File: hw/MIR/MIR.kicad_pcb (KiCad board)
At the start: 2 copper layers, 89.6 x 55 mm, 90 parts, among them J1 CONN_02X08, J10 CONN_01X01, J11 CONN_01X01, J12 CONN_01X01, J13 CONN_01X01, J14 CONN_01X01, J15 CONN_01X01, J16 CONN_01X01, J17 CONN_01X01, J18 CONN_01X01, J19 CONN_01X01, J2 CONN_02X08, J20 CONN_01X01, J21 CONN_01X01, J22 CONN_01X01, J23 CONN_01X01, J24 CONN_01X01, J25 CONN_01X01, J26 CONN_01X01, J27 CONN_01X01, J28 CONN_01X01, J29 CONN_01X01, J3 CONN_01X02, J30 CONN_01X01, J31 CONN_01X01, J32 CONN_01X01, J33 CONN_01X01, J34 CONN_01X01, J35 CONN_01X01, J36 CONN_01X01, J37 CONN_01X01, J38 CONN_01X01, J39 CONN_01X01, J40 CONN_01X01, J41 CONN_02X03, J42 CONN_01X15, J43 CONN_01X15, J44 USB_B_Mini, J9 CONN_01X01, SW1 SwitchPush, U1 ATmega328P-AU, U2 FT230XQ, Y1 16MHz

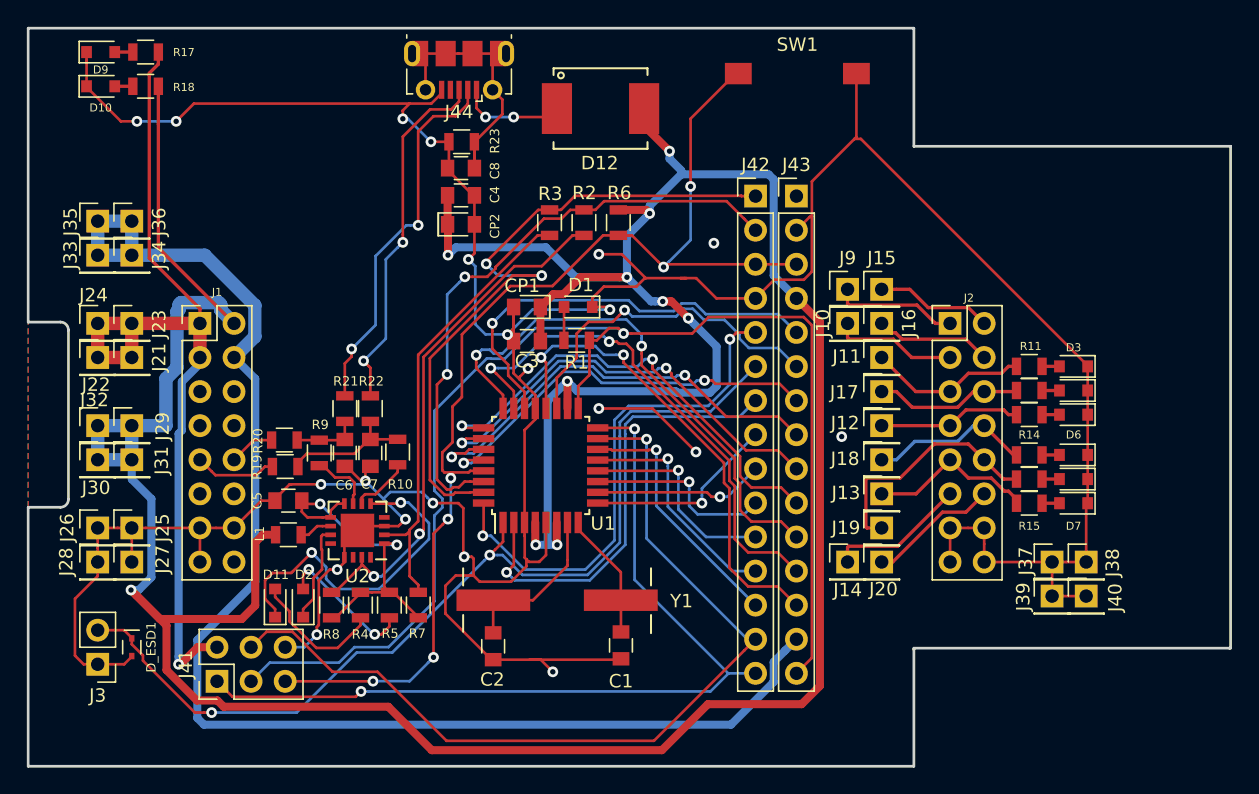
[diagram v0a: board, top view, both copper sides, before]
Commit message: Various fixes in schematics and PCB design
What has been done:

* Change Atmega328p footprint from TQFP to WQFN
* Replace FT230XQ with FT232RQ
* Adapt schematics to new FTDI chip
* Add load resistor for IR LED
* Add missing decoupling capacitors to some VDD pins
* Add cutout for NanoPi microUSB
* Remove unused USB connector
* Remove unused arduino connectors
* Remove not used (for MIR purposees) LEDs indicating state of STM GPIO
* Rename all files to MIR*
* Use only symbols from MIR libraries
* Rearrange texts on F.Mask layer
* Rearrange overlapping texts on F.Silk layer
* Move D_ESD1 further from J3
* Correct SW1 and XTAL footprints

Change-Id: Icd19173fda610c0574442d99b39109bb18bf1090
Signed-off-by: Katarzyna Gorska <k.gorska@samsung.com>
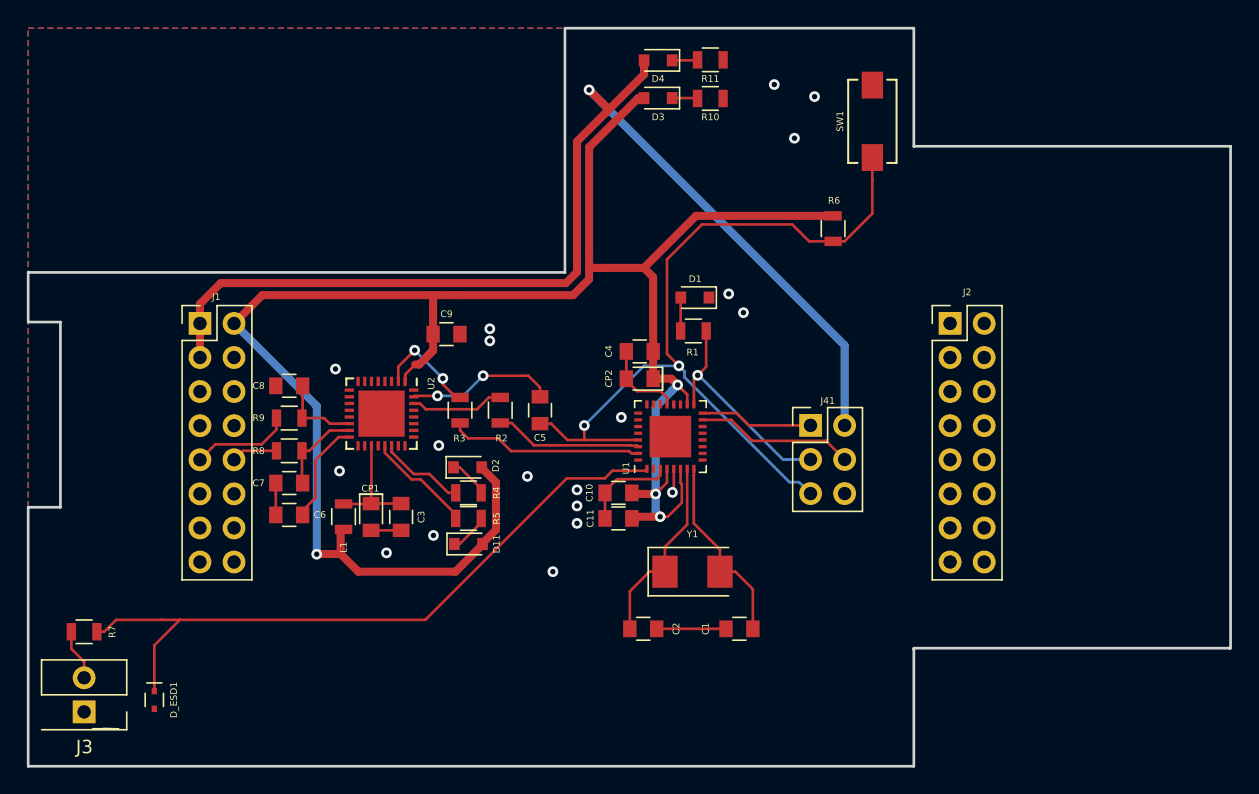
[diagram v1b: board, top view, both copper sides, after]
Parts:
- removed D10, D7: KPT-2012SGC, Diodes_SMD:D_0805
- removed D12: MBRS410L, Muxpi Addon:403AC
- removed D6, D9: KPT-2012EC, Diodes_SMD:D_0805
- removed D8: OSB50805C1E, Diodes_SMD:D_0805
- removed J10, J11, J12, J13, J14, J15, J16, J17, J18, J19, J20, J21, J22, J23, J24, J25, J26, J27, J28, J29, J30, J31, J32, J33, J34, J35, J36, J37, J38, J39, J40, J9: CONN_01X01, Pin_Headers:Pin_Header_Straight_1x01_Pitch2.54mm
- removed J42, J43: CONN_01X15, Muxpi Addon:Pin_Header_Straight_1x15_Pitch2.54mm
- removed J44: USB_B_Mini, Muxpi Addon:USB_Micro-B_Molex-105017-0001
- removed R12, R13, R14, R15, R16, R17, R18: 330R, Resistors_SMD:R_0805
- removed R19, R20, R21, R22: 0, Muxpi Addon:R_0805
- removed R23: 10k, Muxpi Addon:R_0805
- added C10: 0.1uF, MIR:C_0805, F.Cu at (113.3, 169.2)
- added C11: 0.1uF, MIR:C_0805, F.Cu at (113.3, 171.1)
- added C9: 0.1uF, MIR:C_0805, F.Cu at (100.5, 157.4)
- C1, C2, C3, C4, C5: footprint Muxpi Addon:C_0805 -> MIR:C_0805
- C6: value 47pF/50V -> 0.1uF; footprint Muxpi Addon:C_0805 -> MIR:C_0805
- C7: value 47pF/50V -> 47pF; footprint Muxpi Addon:C_0805 -> MIR:C_0805
- C8: value 0.1uF -> 47pF; footprint Muxpi Addon:C_0805 -> MIR:C_0805
- CP1, CP2: footprint Muxpi Addon:C_T_0805 -> MIR:C_T_0805
- D1, D11, D2: footprint Diodes_SMD:D_0805 -> MIR:D_0805
- D3: value KPT-2012EC -> KPT-2012SGC; footprint Diodes_SMD:D_0805 -> MIR:D_0805
- D4: value KPT-2012SGC -> KPT-2012EC; footprint Diodes_SMD:D_0805 -> MIR:D_0805
- D5: value OSB50805C1E -> LED_IR; footprint Diodes_SMD:D_0805 -> MIR:EXTERNAL ELEMENT
- D_ESD1: footprint Muxpi Addon:SOD-523 -> MIR:SOD-523
- J1, J2: footprint Pin_Headers:Pin_Header_Straight_2x08_Pitch2.54mm -> MIR:Pin_Header_Straight_2x08_Pitch2.54mm
- J3: footprint Pin_Headers:Pin_Header_Straight_1x02_Pitch2.54mm -> MIR:Pin_Header_Straight_1x02_Pitch2.54mm_Molex_022232021
- J41: footprint Muxpi Addon:Pin_Header_Straight_2x03_Pitch2.54mm -> MIR:Pin_Header_Straight_2x03_Pitch2.54mm
- L1, R1, R2, R3, R6, R9: footprint Muxpi Addon:R_0805 -> MIR:R_0805
- R10: value 27R -> 330R; footprint Muxpi Addon:R_0805 -> MIR:R_0805
- R11: footprint Resistors_SMD:R_0805 -> MIR:R_0805
- R4, R5: value 560R -> 330R; footprint Muxpi Addon:R_0805 -> MIR:R_0805
- R7: value 10k -> 330R; footprint Muxpi Addon:R_0805 -> MIR:R_0805
- R8: value 10k -> 27R; footprint Muxpi Addon:R_0805 -> MIR:R_0805
- SW1: footprint Muxpi Addon:DTSM-3 -> MIR:DTSM-3
- U1: value ATmega328P-AU -> ATmega328P-MU; footprint Muxpi Addon:TQFP-32_7x7mm_Pitch0.8mm -> MIR:WQFN-32-1EP_5x5mm_Pitch0.5mm
- U2: value FT230XQ -> FT232RQ; footprint Muxpi Addon:QFN-16-1EP_4x4mm_Pitch0.65mm -> MIR:QFN-32-1EP_5x5mm_Pitch0.5mm
- Y1: footprint Muxpi Addon:HC49USM -> MIR:Crystal_SMD_Abracon_ABM3-2pin_5.0x3.2mm_HandSoldering
- moved J41 48.2 mm to (127.6, 164.2), turned to 0 degrees
- moved D4 39.5 mm to (116.2, 137.0)
- moved D5 38.1 mm to (109.5, 157.9), turned to 0 degrees
- moved D3 36.9 mm to (116.2, 139.8)
- moved R10 35.2 mm to (120.1, 139.8), turned to 180 degrees
- moved R11 33.0 mm to (120.1, 137.0), turned to 180 degrees
- moved R7 25.0 mm to (73.5, 179.6), turned to 0 degrees
- moved C8 20.7 mm to (88.8, 161.2), turned to 0 degrees
- moved C5 19.9 mm to (107.4, 163.1), turned to 270 degrees
- moved CP1 19.5 mm to (94.9, 171.0), turned to 270 degrees
- moved C4 17.7 mm to (114.9, 158.7), turned to 180 degrees
- moved CP2 17.6 mm to (114.9, 160.7), turned to 180 degrees
- moved C3 16.1 mm to (97.1, 171.0), turned to 270 degrees
- moved R6 16.0 mm to (129.3, 149.5)
- moved D2 15.9 mm to (102.0, 167.3), turned to 0 degrees
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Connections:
- C3 pad 1: VDD -> /FT_VCC
- C5 pad 2: GND -> /RESET
- C6 pad 1: Net-(C6-Pad1) -> GND
- C6 pad 2: GND -> Net-(C6-Pad2)
- C8 pad 1: Net-(C8-Pad1) -> GND
- C8 pad 2: GND -> Net-(C8-Pad2)
- CP1 pad 1: VDD -> /FT_VCC
- D11 pad 2: Net-(D11-Pad2) -> VDD
- D2 pad 2: Net-(D2-Pad2) -> VDD
- D3 pad 1: GND -> Net-(D3-Pad1)
- D3 pad 2: Net-(D3-Pad2) -> VDD
- D4 pad 1: GND -> Net-(D4-Pad1)
- D4 pad 2: Net-(D4-Pad2) -> +5V
- J1 pad 11: /USB_A+ -> (no net)
- J1 pad 12: /USB_A- -> (no net)
- J1 pad 16: Net-(J1-Pad16) -> (no net)
- J1 pad 4: +3V3 -> (no net)
- J1 pad 5: /SDA -> (no net)
- J1 pad 6: /SCL -> (no net)
- J1 pad 7: /PI_UART_TX -> (no net)
- J1 pad 8: /PI_UART_RX -> (no net)
- J2 pad 1: /SPI_CLK -> (no net)
- J2 pad 10: /ST_GPIO_3 -> (no net)
- J2 pad 11: /ADC1 -> (no net)
- J2 pad 12: /ADC2 -> (no net)
- J2 pad 2: /SPI_MOSI -> (no net)
- J2 pad 3: /SPI_CS -> (no net)
- J2 pad 4: /SPI_MISO -> (no net)
- J2 pad 5: /PI_GPIO_1 -> (no net)
- J2 pad 6: /PI_GPIO_2 -> (no net)
- J2 pad 7: /PI_GPIO_3 -> (no net)
- J2 pad 8: /ST_GPIO_1 -> (no net)
- J2 pad 9: /ST_GPIO_2 -> (no net)
- J3 pad 2: /D3 -> Net-(J3-Pad2)
- L1 pad 1: Net-(L1-Pad1) -> /FT_VCC
- R10 pad 1: Net-(C7-Pad1) -> GND
- R10 pad 2: Net-(R10-Pad2) -> Net-(D3-Pad1)
- R11 pad 1: /PI_GPIO_1 -> GND
- R11 pad 2: Net-(D3-Pad2) -> Net-(D4-Pad1)
- R4 pad 1: Net-(C5-Pad1) -> Net-(R4-Pad1)
- R4 pad 2: Net-(D11-Pad2) -> Net-(D2-Pad1)
- R5 pad 1: Net-(C5-Pad1) -> Net-(R5-Pad1)
- R5 pad 2: Net-(D2-Pad2) -> Net-(D11-Pad1)
- R7 pad 1: /TX -> Net-(J3-Pad2)
- R7 pad 2: Net-(C5-Pad1) -> /D3
- R8 pad 1: /RX -> /USB_B-
- R8 pad 2: Net-(C5-Pad1) -> Net-(C7-Pad1)
- R9 pad 1: Net-(C6-Pad1) -> /USB_B+
- R9 pad 2: Net-(R9-Pad2) -> Net-(C8-Pad2)
- U1 pad 10: /D6 -> (no net)
- U1 pad 11: /D7 -> (no net)
- U1 pad 12: /D8 -> (no net)
- U1 pad 13: /D9 -> (no net)
- U1 pad 14: /D10 -> (no net)
- U1 pad 19: /A6 -> (no net)
- U1 pad 2: /D4 -> (no net)
- U1 pad 20: /AREF -> (no net)
- U1 pad 22: /A7 -> (no net)
- U1 pad 23: /A0 -> (no net)
- U1 pad 24: /A1 -> (no net)
- U1 pad 25: /A2 -> (no net)
- U1 pad 26: /A3 -> (no net)
- U1 pad 27: /A4 -> (no net)
- U1 pad 28: /A5 -> (no net)
- U1 pad 32: /D2 -> (no net)
- U1 pad 9: /D5 -> (no net)
- U2 pad 1: Net-(C5-Pad1) -> VDD
- U2 pad 10: Net-(L1-Pad1) -> (no net)
- U2 pad 11: Net-(D2-Pad1) -> (no net)
- U2 pad 12: Net-(U2-Pad12) -> (no net)
- U2 pad 13: GND -> (no net)
- U2 pad 14: Net-(U2-Pad14) -> Net-(C8-Pad2)
- U2 pad 15: /RX -> Net-(C7-Pad1)
- U2 pad 16: Net-(U2-Pad16) -> Net-(C6-Pad2)
- U2 pad 3: GND -> (no net)
- U2 pad 4: Net-(U2-Pad4) -> GND
- U2 pad 5: Net-(D11-Pad1) -> (no net)
- U2 pad 6: Net-(R10-Pad2) -> (no net)
- U2 pad 7: Net-(R9-Pad2) -> (no net)
- U2 pad 8: Net-(C5-Pad1) -> (no net)
- U2 pad 9: Net-(C5-Pad1) -> (no net)
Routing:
- net GND: track 307.9 -> 25.6 mm, vias 21 -> 19
- net VDD: track 272.2 -> 147.7 mm, vias 10 -> 4
- net +3V3: track 103.1 -> 0.00 mm
- net /D13-SCK: track 97.4 -> 16.9 mm
- net /D12-MISO: track 64.8 -> 8.42 mm, vias 2 -> 0
- net /D11-MOSI: track 66.2 -> 11.8 mm, vias 1 -> 0
- net /A1: track 40.1 -> 0.00 mm, vias 2 -> 0
- net /A0: track 38.5 -> 0.00 mm, vias 2 -> 0
- net /D2: track 38.4 -> 0.00 mm, vias 2 -> 0
- net /D1-TX: track 51.3 -> 14.5 mm, vias 2 -> 0
- net /AREF: track 36.0 -> 0.00 mm, vias 2 -> 0
- net /A2: track 35.1 -> 0.00 mm, vias 2 -> 0
- net /D0-RX: track 45.5 -> 11.0 mm, vias 2 -> 0
- net /D4: track 33.5 -> 0.00 mm, vias 1 -> 0
- net /A4: track 33.3 -> 0.00 mm, vias 2 -> 0
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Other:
- outline, holes or cut-outs redrawn
- board text removed: "+3V3"
- board text removed: "+5V"
- board text removed: "ADC1"
- board text removed: "ADC2"
- board text removed: "CLK"
- board text removed: "CS"
- board text removed: "GND"
- board text removed: "MI"
- board text removed: "MO"
- board text removed: "PI GPIO 1"
- board text removed: "PI GPIO 2"
- board text removed: "PI GPIO 3"
- board text removed: "PI1"
- board text removed: "PI2"
- board text removed: "PI3"
- board text removed: "SCL"
- board text removed: "SDA"
- board text removed: "ST GPIO 1"
- board text removed: "ST GPIO 2"
- board text removed: "ST GPIO 3"
- board text removed: "ST1"
- board text removed: "ST2"
- board text removed: "ST3"
- board text removed: "UA+"
- board text removed: "UA-"
- board text removed: "UB+"
- board text removed: "UB-"
- board text removed: "VDD"
